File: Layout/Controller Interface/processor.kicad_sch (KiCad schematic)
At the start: 15 parts, among them J1 USB_C_Receptacle_USB2.0, SW2 SW_Push, SW3 SW_Push, SW4 SW_Push, U1 RP2040, U3 W25X40CLSN, Y1 12MHz

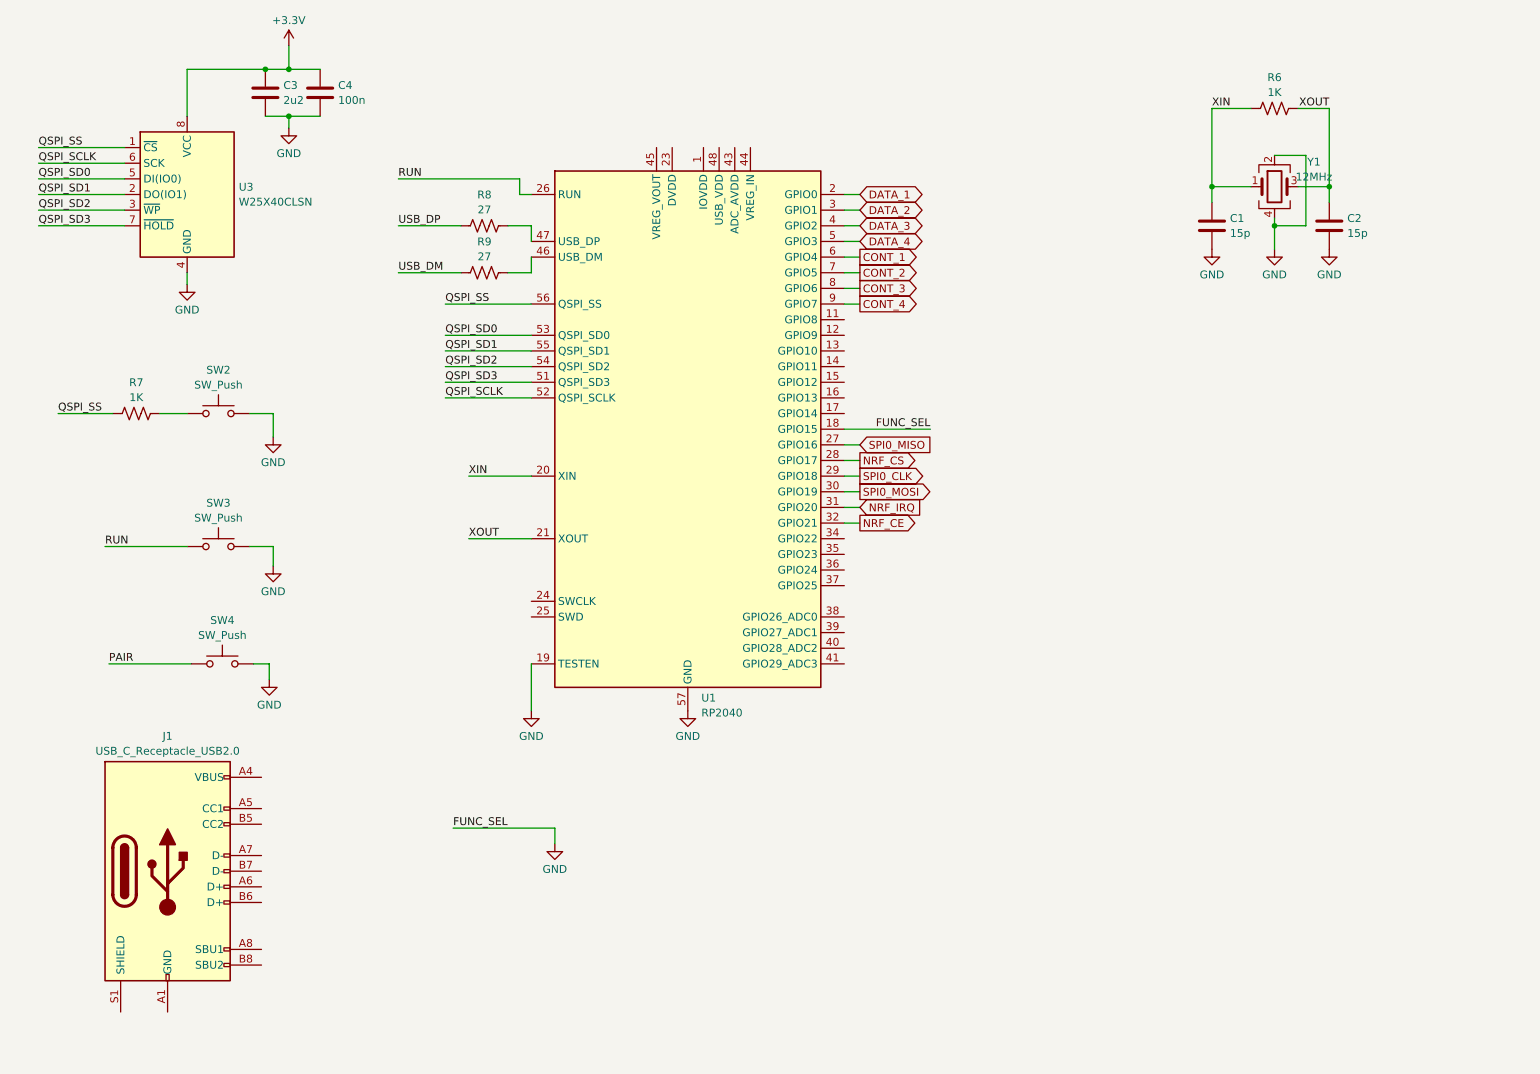
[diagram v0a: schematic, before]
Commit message: Schematic updates
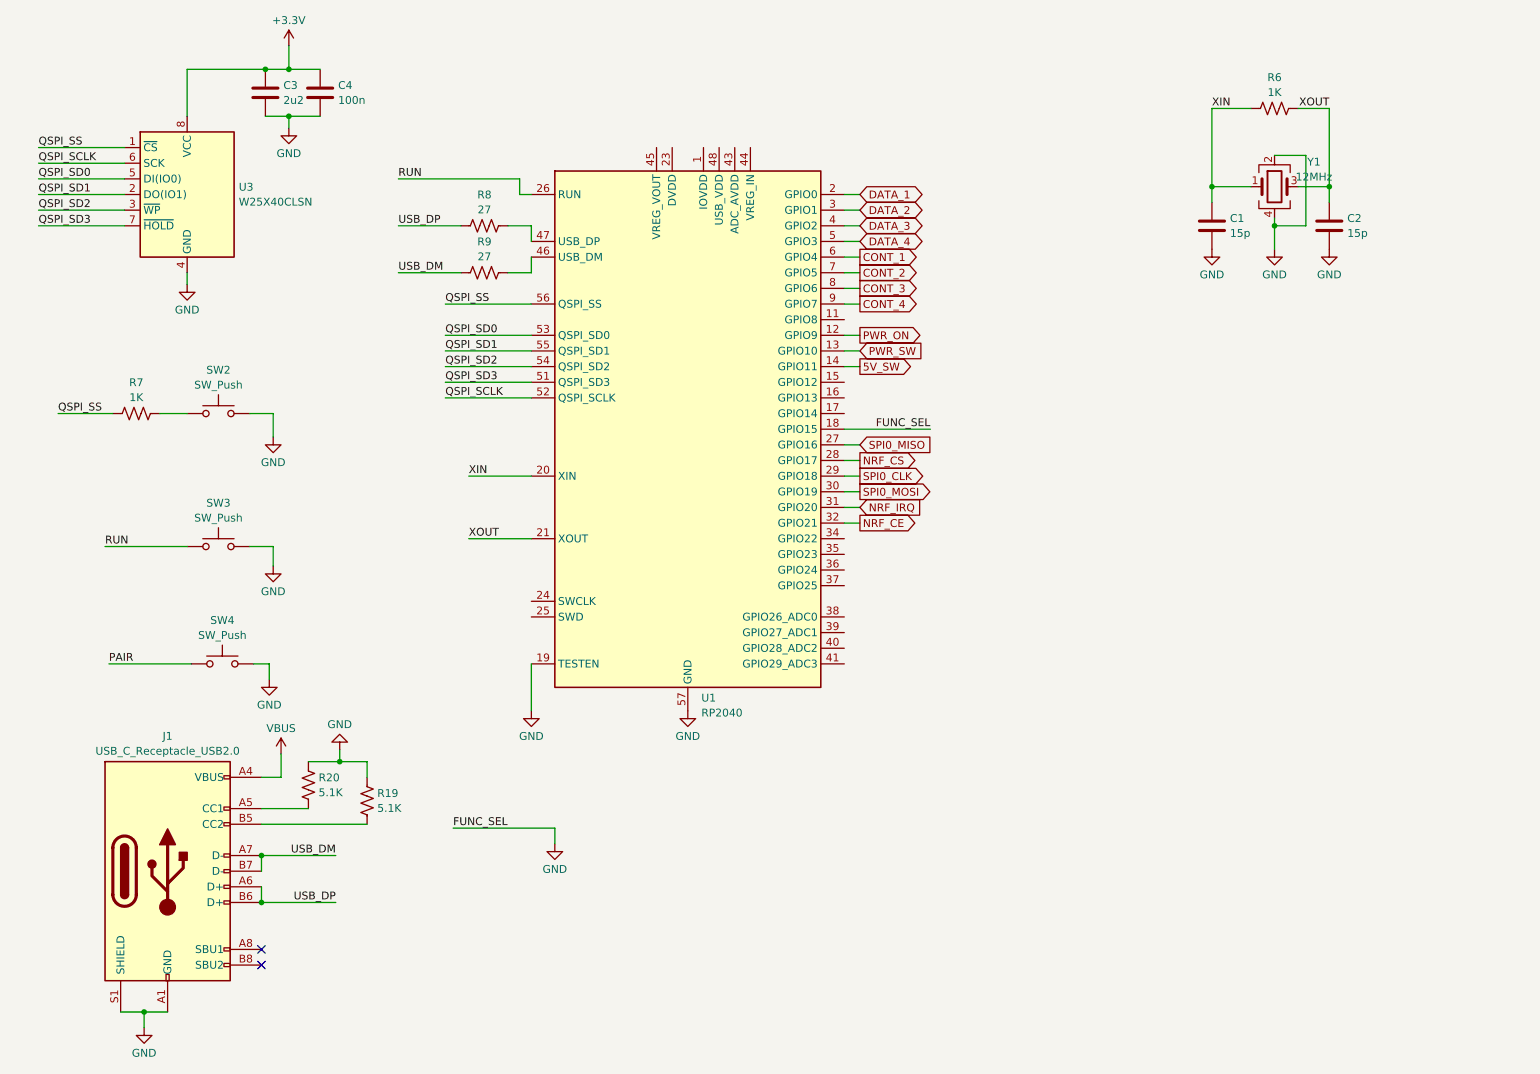
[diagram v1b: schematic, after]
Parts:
- added R19, R20: 5.1K, Resistor_SMD:R_0805_2012Metric, symbol Device:R_US
- C1, C2, C3, C4: footprint (none) -> Capacitor_SMD:C_0805_2012Metric
- J1: footprint (none) -> Connector_USB:USB_C_Receptacle_HRO_TYPE-C-31-M-12
- R6, R7, R8, R9: footprint (none) -> Resistor_SMD:R_0805_2012Metric
- SW2, SW3, SW4: footprint (none) -> Button_Switch_SMD:SW_SPST_TL3342
- Y1: footprint (none) -> Crystal:Crystal_SMD_3225-4Pin_3.2x2.5mm_HandSoldering
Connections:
- net GND: now also J1.A1 (GND), J1.A12 (GND), J1.B1 (GND), J1.B12 (GND), J1.S1 (SHIELD), R19.2, R20.2
- net USB_DM: now also J1.A7 (D-), J1.B7 (D-)
- net USB_DP: now also J1.A6 (D+), J1.B6 (D+)
- net PWR_ON: now reaches U1.12 (GPIO9)
- net PWR_SW: now reaches U1.13 (GPIO10)
- net 5V_SW: now reaches U1.14 (GPIO11)
- net VBUS: now reaches J1.A4 (VBUS), J1.A9 (VBUS), J1.B4 (VBUS), J1.B9 (VBUS)
- net at J1.A5 (CC1): now also R20.1
- net at J1.B5 (CC2): now also R19.1
- no-connect marks 0 -> 2

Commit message: Completed schematic and layout
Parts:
- removed R19, R20: 5.1K, Resistor_SMD:R_0805_2012Metric, symbol Device:R_US
- removed SW2: SW_Push, Button_Switch_SMD:SW_SPST_TL3342, symbol Switch:SW_Push
- removed U1: RP2040, Package_DFN_QFN:QFN-56-1EP_7x7mm_P0.4mm_EP3.2x3.2mm, symbol MCU_RaspberryPi:RP2040
- removed U3: W25X40CLSN, Package_SO:SOIC-8_3.9x4.9mm_P1.27mm, symbol Memory_Flash:W25X40CLSN
- removed Y1: 12MHz, Crystal:Crystal_SMD_3225-4Pin_3.2x2.5mm_HandSoldering, symbol Device:Crystal_GND24
- added C11, C15: 2u2, Capacitor_SMD:C_0603_1608Metric, symbol Device:C
- added C12, C13, C14, C16, C17, C18, C19, C20: 100n, Capacitor_SMD:C_0603_1608Metric, symbol Device:C
- added D1: LED, LED_SMD:LED_0805_2012Metric, symbol Device:LED
- added R13: 1K, Resistor_SMD:R_0603_1608Metric, symbol Device:R_US
- added R4: 100, Resistor_SMD:R_0805_2012Metric, symbol Device:R_US
- added U1: W25Q32JVSS, Package_SO:SOIC-8_5.23x5.23mm_P1.27mm, symbol Memory_Flash:W25Q32JVSS
- added U2: RP2040, Package_DFN_QFN:QFN-56-1EP_7x7mm_P0.4mm_EP3.2x3.2mm, symbol MCU_RaspberryPi:RP2040
- added Y2: Crystal_GND24, Crystal:Crystal_SMD_Abracon_ABM8G-4Pin_3.2x2.5mm, symbol Device:Crystal_GND24
- C1: value 15p -> 100n; footprint Capacitor_SMD:C_0805_2012Metric -> Capacitor_SMD:C_0603_1608Metric
- C2: value 15p -> 2u2; footprint Capacitor_SMD:C_0805_2012Metric -> Capacitor_SMD:C_0603_1608Metric
- C3: value 2u2 -> 15p; footprint Capacitor_SMD:C_0805_2012Metric -> Capacitor_SMD:C_0603_1608Metric
- C4: value 100n -> 15p; footprint Capacitor_SMD:C_0805_2012Metric -> Capacitor_SMD:C_0603_1608Metric
- J1: footprint Connector_USB:USB_C_Receptacle_HRO_TYPE-C-31-M-12 -> Connector_USB:USB_C_Receptacle_GCT_USB4105-xx-A_16P_TopMnt_Horizontal
- R6, R7: value 1K -> 27; footprint Resistor_SMD:R_0805_2012Metric -> Resistor_SMD:R_0603_1608Metric
- R8, R9: value 27 -> 5K1; footprint Resistor_SMD:R_0805_2012Metric -> Resistor_SMD:R_0603_1608Metric
- SW3: value SW_Push -> SW_PAIR
- SW4: value SW_Push -> SW_BOOT
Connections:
- net RUN is gone; now on net PAIR: SW3.1
- net +3.3V: now also C1.1, C2.1, C11.1, C12.1, C13.1, C14.1, C17.1, C18.1, C19.1, U1.8 (VCC), U2.1 (IOVDD), U2.10 (IOVDD), U2.22 (IOVDD), U2.33 (IOVDD), U2.42 (IOVDD), U2.44 (VREG_IN), U2.49 (IOVDD); no longer C3.1, C4.1
- net CONT_1: now also U2.2 (GPIO0)
- net CONT_2: now also U2.41 (GPIO29_ADC3)
- net CONT_3: now also U2.14 (GPIO11)
- net CONT_4: now also U2.29 (GPIO18)
- net DATA_1: now also U2.3 (GPIO1)
- net DATA_2: now also U2.40 (GPIO28_ADC2)
- net DATA_3: now also U2.13 (GPIO10)
- net DATA_4: now also U2.30 (GPIO19)
- net GND: now also C4.1, R8.2, R9.2, C11.2, C12.2, C13.2, C14.2, C15.2, C16.2, C17.2, C18.2, C19.2, C20.2, D1.1 (K), U1.4 (GND), U2.19 (TESTEN), U2.43 (ADC_AVDD), U2.57 (GND), Y2.2, Y2.4; no longer C4.2
- net NRF_CE: now also U2.27 (GPIO16)
- net NRF_CS: now also U2.16 (GPIO13)
- net NRF_IRQ: now also U2.28 (GPIO17)
- net PAIR: now also U2.4 (GPIO2); no longer SW4.1
- net PWR_ON: now also U2.38 (GPIO26_ADC0)
- net PWR_SW: now also U2.39 (GPIO27_ADC1)
- net QSPI_SCLK: now also U1.6 (CLK), U2.52 (QSPI_SCLK)
- net QSPI_SD0: now also U1.5 (DI(IO0)), U2.53 (QSPI_SD0)
- net QSPI_SD1: now also U1.2 (DO(IO1)), U2.55 (QSPI_SD1)
- net QSPI_SD2: now also U1.3 (IO2), U2.54 (QSPI_SD2)
- net QSPI_SD3: now also U1.7 (IO3), U2.51 (QSPI_SD3)
- net QSPI_SS: now also R13.1, U1.1 (~{CS}), U2.56 (QSPI_SS); no longer R7.1
- net SPI0_CLK: now also U2.17 (GPIO14)
- net SPI0_MISO: now also U2.15 (GPIO12)
- net SPI0_MOSI: now also U2.18 (GPIO15)
- net USB_DM: now also R6.2, U2.46 (USB_DM); no longer J1.A7 (D-), J1.B7 (D-), R9.1
- net USB_DP: now also R7.2, U2.47 (USB_DP); no longer J1.A6 (D+), J1.B6 (D+), R8.1
- net at J1.A5 (CC1): now also R8.1
- net at J1.B5 (CC2): now also R9.1
- net XIN: no longer names the net of R6.1
- net XIN: now also J1.A7 (D-), J1.B7 (D-); no longer C1.1
- removed net XOUT: C2.1, R6.2
- new net: C3.1, U2.20 (XIN), Y2.1
- new net: C4.2, U2.21 (XOUT), Y2.3
- new net: J1.A6 (D+), J1.B6 (D+), R7.1
- new net: R13.2, SW4.1
- new net: D1.2 (A), R4.2
- new net +1V1: C15.1, C16.1, C20.1, U2.23 (DVDD), U2.45 (VREG_VOUT), U2.48 (USB_VDD), U2.50 (DVDD)
- new net PWR_LED: R4.1, U2.5 (GPIO3)
- new net RX_LED: U2.7 (GPIO5)
- new net TX_LED: U2.6 (GPIO4)
- no-connect marks 2 -> 5

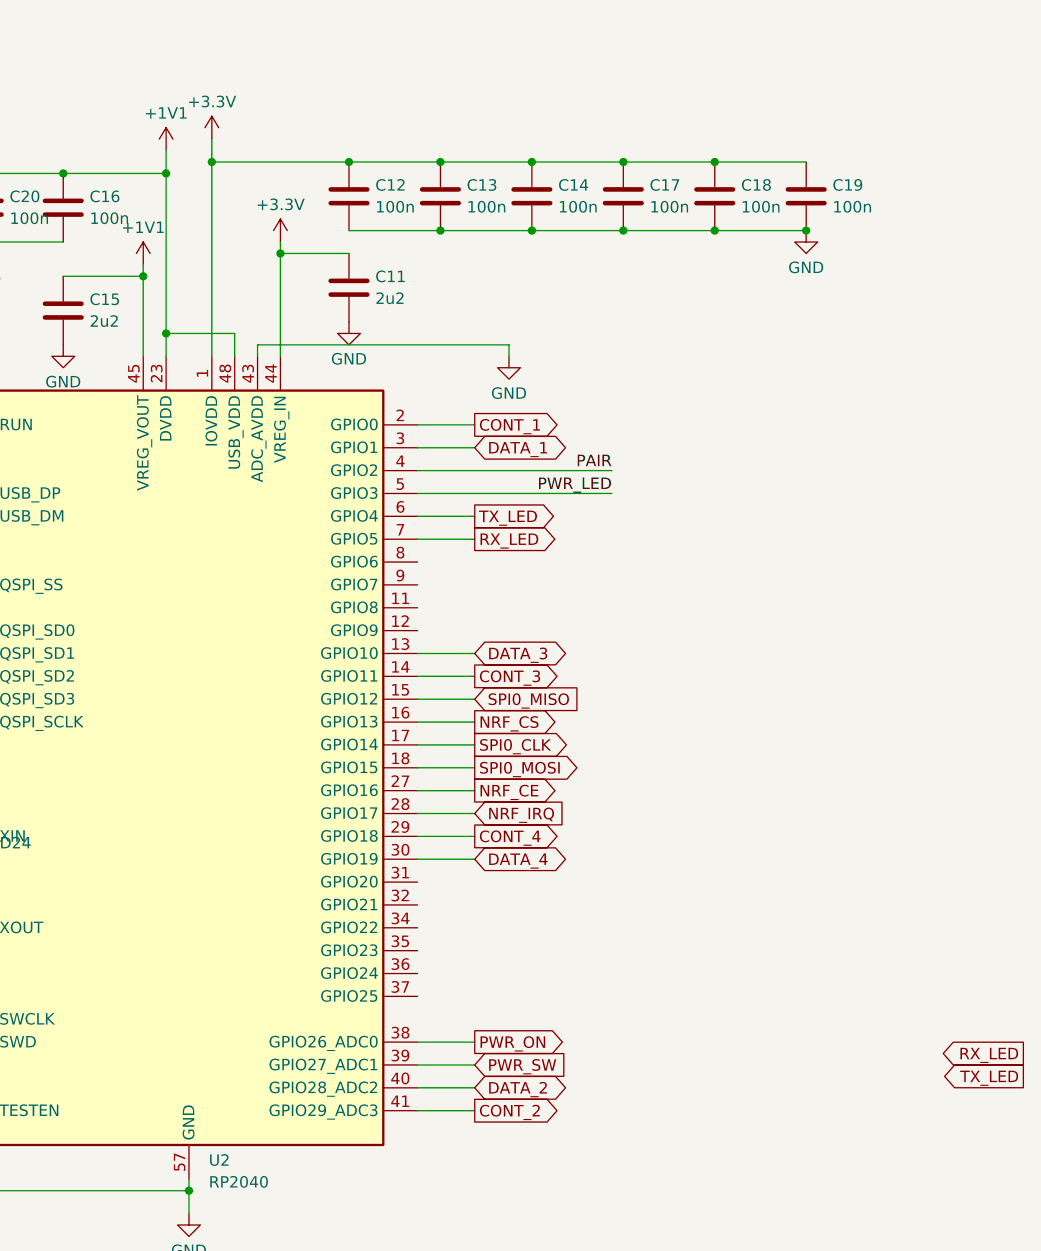
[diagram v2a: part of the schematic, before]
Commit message: Schematic/PCB fixes
Fix VUSB supply. Add cut out for antenna wire.
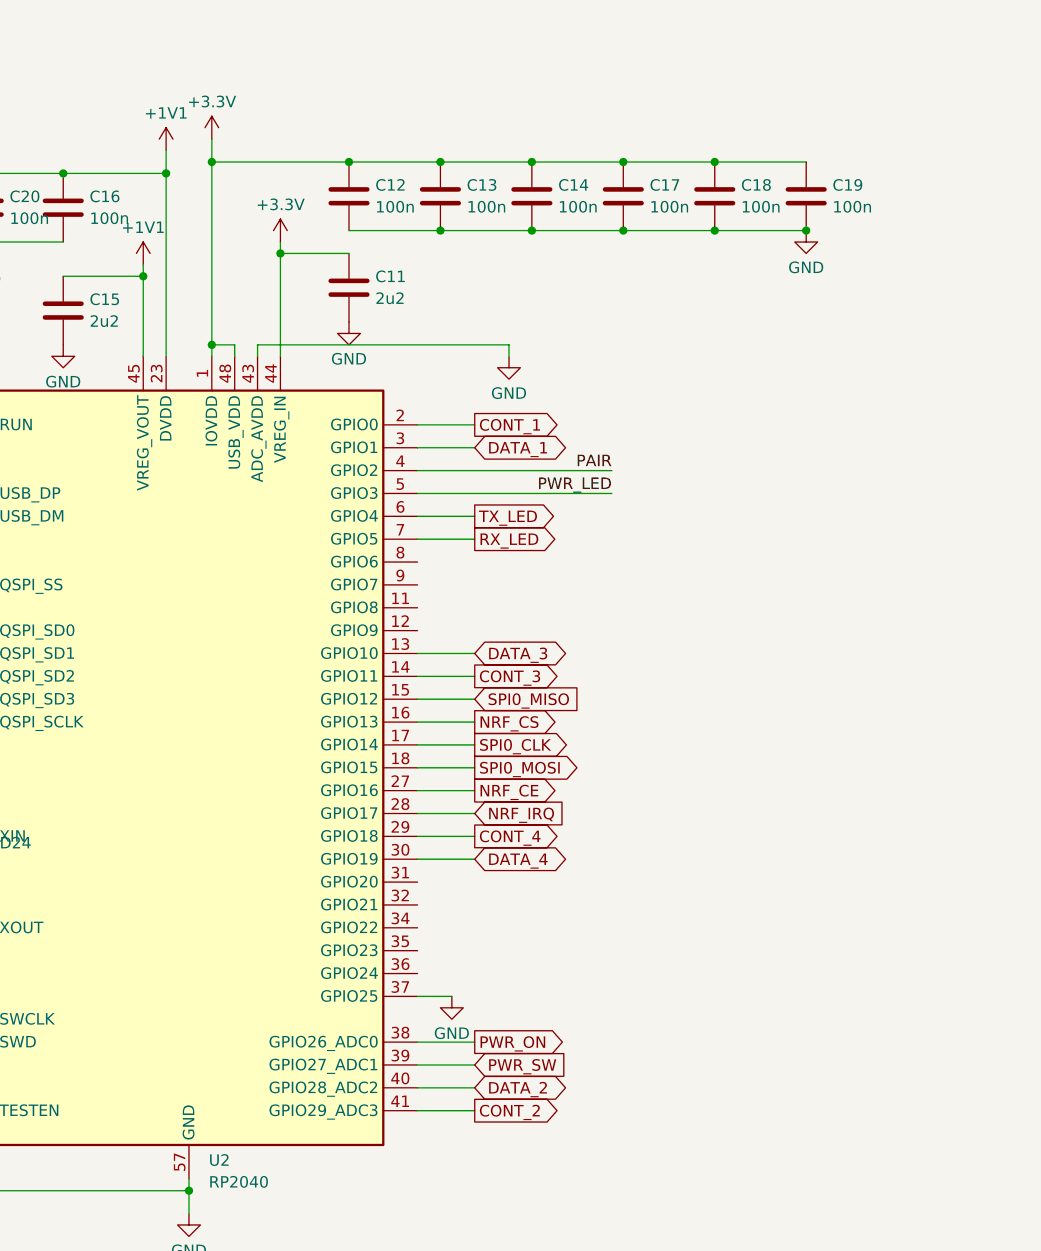
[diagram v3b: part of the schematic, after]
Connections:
- net +1V1: no longer U2.48 (USB_VDD)
- net +3.3V: now also U2.48 (USB_VDD)
- net GND: now also U2.37 (GPIO25)
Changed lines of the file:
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@@
   (junction (at 187.96 46.99) (diameter 0) (color 0 0 0 0)
   )
-  (junction (at 157.48 58.42) (diameter 0) (color 0 0 0 0)
-  )
   (junction (at 160.02 153.67) (diameter 0) (color 0 0 0 0)
   )
@@
   )
   (junction (at 228.6 46.99) (diameter 0) (color 0 0 0 0)
+  )
+  (junction (at 162.56 59.69) (diameter 0) (color 0 0 0 0)
   )
   (junction (at 111.76 127) (diameter 0) (color 0 0 0 0)
@@
     (stroke (width 0) (type default))
   )
-  (wire (pts (xy 165.1 58.42) (xy 157.48 58.42))
-    (stroke (width 0) (type default))
-  )
   (wire (pts (xy 185.42 81.28) (xy 191.77 81.28))
     (stroke (width 0) (type default))
@@
     (stroke (width 0) (type default))
   )
-  (wire (pts (xy 162.56 60.96) (xy 162.56 39.37))
+  (wire (pts (xy 162.56 60.96) (xy 162.56 59.69))
     (stroke (width 0) (type default))
   )
@@
     (stroke (width 0) (type default))
   )
-  (wire (pts (xy 157.48 40.64) (xy 157.48 58.42))
+  (wire (pts (xy 157.48 40.64) (xy 157.48 60.96))
     (stroke (width 0) (type default))
   )
@@
     (stroke (width 0) (type default))
   )
+  (wire (pts (xy 185.42 132.08) (xy 189.23 132.08))
+    (stroke (width 0) (type default))
+  )
   (wire (pts (xy 111.76 130.81) (xy 111.76 135.89))
     (stroke (width 0) (type default))
@@
     (stroke (width 0) (type default))
   )
+  (wire (pts (xy 165.1 59.69) (xy 162.56 59.69))
+    (stroke (width 0) (type default))
+  )
   (wire (pts (xy 123.19 91.44) (xy 134.62 91.44))
     (stroke (width 0) (type default))
@@
     (stroke (width 0) (type default))
   )
+  (wire (pts (xy 162.56 59.69) (xy 162.56 39.37))
+    (stroke (width 0) (type default))
+  )
   (wire (pts (xy 185.42 104.14) (xy 191.77 104.14))
     (stroke (width 0) (type default))
@@
     (stroke (width 0) (type default))
   )
+  (wire (pts (xy 165.1 60.96) (xy 165.1 59.69))
+    (stroke (width 0) (type default))
+  )
   (wire (pts (xy 185.42 142.24) (xy 191.77 142.24))
     (stroke (width 0) (type default))
@@
     (stroke (width 0) (type default))
   )
-  (wire (pts (xy 157.48 58.42) (xy 157.48 60.96))
-    (stroke (width 0) (type default))
-  )
   (wire (pts (xy 185.42 106.68) (xy 191.77 106.68))
     (stroke (width 0) (type default))
@@
   )
   (wire (pts (xy 111.76 127) (xy 111.76 130.81))
-    (stroke (width 0) (type default))
-  )
-  (wire (pts (xy 165.1 60.96) (xy 165.1 58.42))
     (stroke (width 0) (type default))
   )
@@
     )
   )
-  (global_label "RX_LED" (shape output) (at 252.73 138.43 180) (fields_autoplaced)
-    (effects (font (size 1.27 1.27)) (justify right))
-    (property "Intersheetrefs" "${INTERSHEET_REFS}" (at 242.8506 138.43 0)
-      (effects (font (size 1.27 1.27)) (justify right) hide)
-    )
-  )
   (global_label "DATA_2" (shape bidirectional) (at 191.77 142.24 0) (fields_autoplaced)
     (effects (font (size 1.27 1.27)) (justify left))
@@
     (property "Intersheetrefs" "${INTERSHEET_REFS}" (at 201.8309 96.52 0)
       (effects (font (size 1.27 1.27)) (justify left) hide)
-    )
-  )
-  (global_label "TX_LED" (shape output) (at 252.73 140.97 180) (fields_autoplaced)
-    (effects (font (size 1.27 1.27)) (justify right))
-    (property "Intersheetrefs" "${INTERSHEET_REFS}" (at 243.153 140.97 0)
-      (effects (font (size 1.27 1.27)) (justify right) hide)
     )
   )
@@
         )
       )
+    )
+  )
+  (symbol (lib_id "power:GND") (at 189.23 132.08 0) (unit 1)
+    (in_bom yes) (on_board yes) (dnp no) (fields_autoplaced)
+    (property "Reference" "#PWR059" (at 189.23 138.43 0)
+      (effects (font (size 1.27 1.27)) hide)
+    )
+    (property "Value" "GND" (at 189.23 136.2131 0)
+      (effects (font (size 1.27 1.27)))
+    )
+    (property "Footprint" "" (at 189.23 132.08 0)
+      (effects (font (size 1.27 1.27)) hide)
+    )
+    (property "Datasheet" "" (at 189.23 132.08 0)
+      (effects (font (size 1.27 1.27)) hide)
+    )
+    (pin "1")
+    (instances
+      (project "Controller Interface"
+        (path "/debf4462-021e-4805-bcd2-6130c1f65c4c/b67b8a11-cf45-4531-a24a-54934a9624a8"
+          (reference "#PWR059") (unit 1)
+        )
+      )
